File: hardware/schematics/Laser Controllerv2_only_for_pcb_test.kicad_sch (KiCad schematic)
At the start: 116 parts, among them J1 SD Card Module (6-pin, 2.54mm), J2 12.6V IN (BUCK), J3 PWR IN Galvo, J4 FAN1 12V IN, J5 FAN1, J6 FAN2 12V IN, J7 FAN2, U1 ESP32-S3-N16R8-DevKit, U10 DS18B20 connector, U12 OPA4134UA_2K5, U13 Galvo Input, U15 6N137, U16 6N137, U17 6N137, U2 DAC8562SDGST, U3 TTL_RGB Blue, U4 TTL_RGB Red, U5 TTL_RGB Green, U6 DS18B20 connector, U7 DS18B20 connector, U8 DS18B20 connector, U9 DS18B20 connector

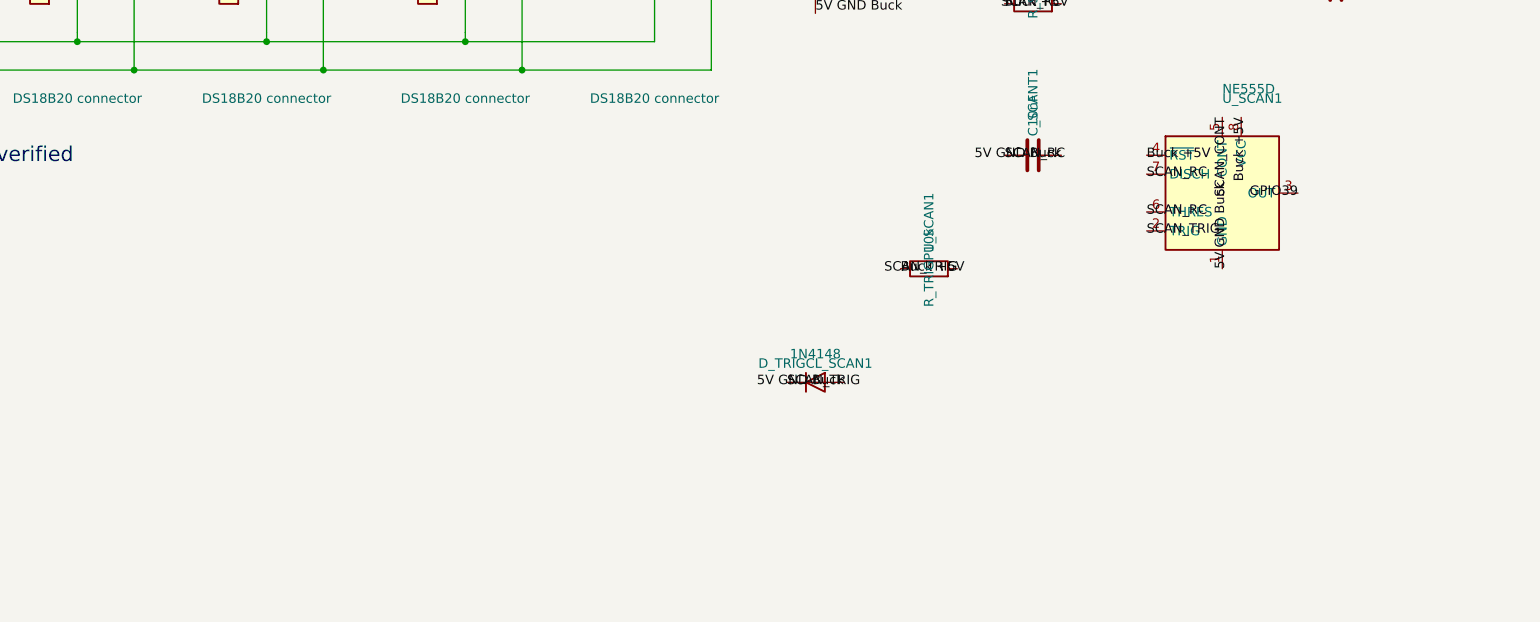
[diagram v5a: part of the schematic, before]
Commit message: fix(hw): buffer scan-status GPIO in v2.0.4
Remove direct 5 V timer drive of GPIO39 while preserving polarity.
Keep the draft unreleased pending safety and physical validation.
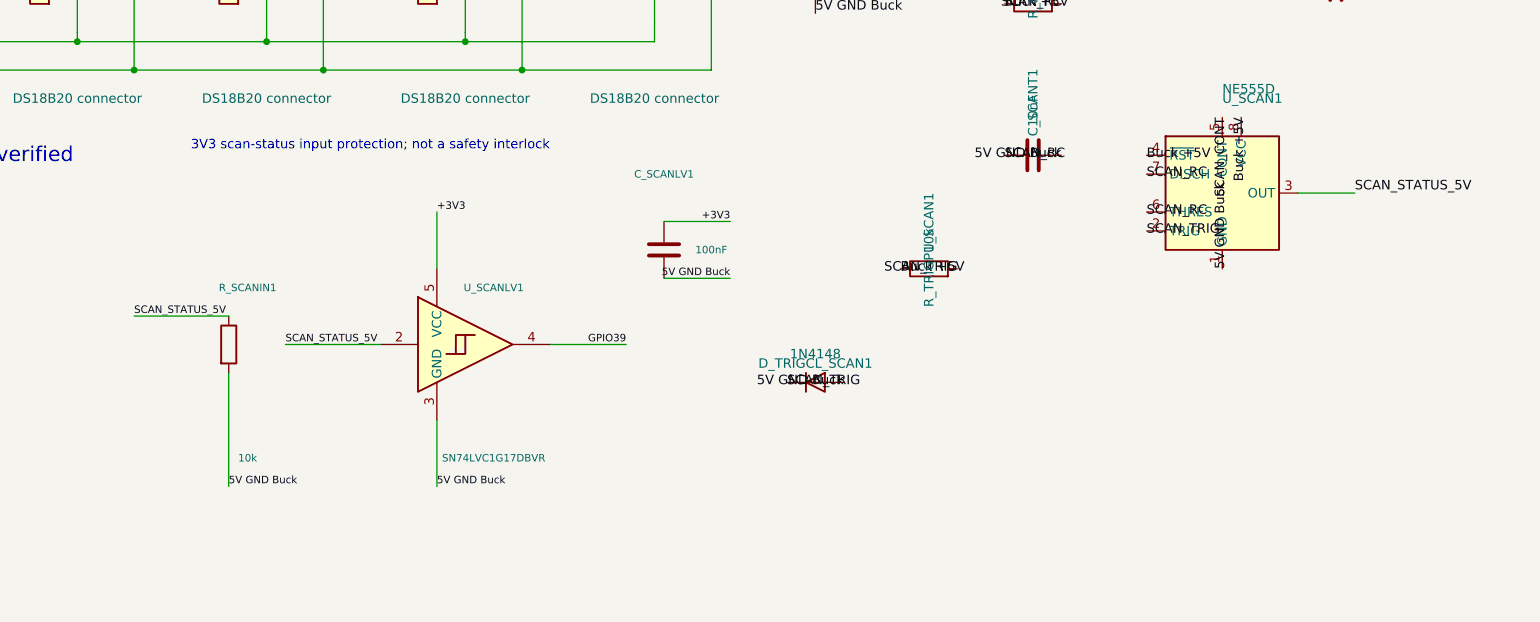
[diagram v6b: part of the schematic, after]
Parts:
- added C_SCANLV1: 100nF, Capacitor_SMD:C_1206_3216Metric, symbol Device:C
- added R_SCANIN1: 10k, Resistor_SMD:R_1206_3216Metric, symbol Device:R
- added U_SCANLV1: SN74LVC1G17DBVR, Package_TO_SOT_SMD:SOT-23-5, symbol 74xGxx:74LVC1G17
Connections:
- net +3V3: now also C_SCANLV1.1, U_SCANLV1.5 (VCC)
- net 5V GND Buck: now also C_SCANLV1.2, R_SCANIN1.2, U_SCANLV1.3 (GND)
- net GPIO39: now also U_SCANLV1.4; no longer U_SCAN1.3 (OUT)
- new net SCAN_STATUS_5V: R_SCANIN1.1, U_SCAN1.3 (OUT), U_SCANLV1.2
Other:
- note added: "3V3 scan-status input protection; not a safety interlock"
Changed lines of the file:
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@@
 		(title "GalvOS ESP32 Laser Controller - V2 engineering review")
 		(date "2026-09-14")
-		(rev "V2.0.3 DRAFT - NOT FOR FABRICATION")
+		(rev "V2.0.4 DRAFT - NOT FOR FABRICATION")
 	)
 	(rectangle
@@
 		)
 	)
-	(label "GPIO39"
-		(at 554.99 330.2 180)
+(label "SCAN_STATUS_5V"
+		(at 562.61 330.2 0)
 		(effects
 			(font
 				(size 1.27 1.27)
 			)
-			(justify right)
+			(justify left bottom)
 		)
 	)
+(wire (pts (xy 554.99 330.2) (xy 562.61 330.2)) (stroke (width 0) (type default)))
 	(label "Buck +5V"
 		(at 389.89 77.47 0)
@@
 		)
 	)
+(symbol (lib_id "74xGxx:74LVC1G17") (at 444.5 350.52 0) (unit 1) (in_bom yes) (on_board yes) (dnp no)
+(property "Reference" "U_SCANLV1" (at 447.04 342.9 0) (effects (font (size 1 1))))
+(property "Value" "SN74LVC1G17DBVR" (at 447.04 365.76 0) (effects (font (size 1 1))))
+(property "Footprint" "Package_TO_SOT_SMD:SOT-23-5" (at 444.5 350.52 0) (hide yes) (effects (font (size 1 1))))
+(property "Datasheet" "https://www.ti.com/lit/ds/symlink/sn74lvc1g17.pdf" (at 444.5 350.52 0) (hide yes) (effects (font (size 1 1))))
+(property "Manufacturer" "Texas Instruments" (at 444.5 350.52 0) (hide yes) (effects (font (size 1 1))))
+(property "MPN" "SN74LVC1G17DBVR" (at 444.5 350.52 0) (hide yes) (effects (font (size 1 1))))
+(property "Layout" "5V-tolerant noninverting buffer; supply from MCU +3V3; local C_SCANLV1 to MCU power ground. Not an independent laser interlock." (at 444.5 350.52 0) (hide yes) (effects (font (size 1 1))))
+(instances (project "Laser Controllerv2_only_for_pcb_test" (path "/d54d297e-dc0d-4b80-be70-d4630411b2f0" (reference "U_SCANLV1") (unit 1)))))
+(symbol (lib_id "Device:R") (at 411.48 350.52 0) (unit 1) (in_bom yes) (on_board yes) (dnp no)
+(property "Reference" "R_SCANIN1" (at 414.02000000000004 342.9 0) (effects (font (size 1 1))))
+(property "Value" "10k" (at 414.02000000000004 365.76 0) (effects (font (size 1 1))))
+(property "Footprint" "Resistor_SMD:R_1206_3216Metric" (at 411.48 350.52 0) (hide yes) (effects (font (size 1 1))))
+(property "Tolerance" "1%" (at 411.48 350.52 0) (hide yes) (effects (font (size 1 1))))
+(property "Power" "0.25W" (at 411.48 350.52 0) (hide yes) (effects (font (size 1 1))))
+(property "Layout" "Bias the buffer input LOW if the timer output is disconnected." (at 411.48 350.52 0) (hide yes) (effects (font (size 1 1))))
+(instances (project "Laser Controllerv2_only_for_pcb_test" (path "/d54d297e-dc0d-4b80-be70-d4630411b2f0" (reference "R_SCANIN1") (unit 1)))))
+(symbol (lib_id "Device:C") (at 469.9 337.82 0) (unit 1) (in_bom yes) (on_board yes) (dnp no)
+(property "Reference" "C_SCANLV1" (at 469.9 327.66 0) (effects (font (size 1 1))))
+(property "Value" "100nF" (at 476.25 337.82 0) (effects (font (size 1 1))))
+(property "Footprint" "Capacitor_SMD:C_1206_3216Metric" (at 469.9 337.82 0) (hide yes) (effects (font (size 1 1))))
+(property "Voltage" "50V" (at 469.9 337.82 0) (hide yes) (effects (font (size 1 1))))
+(property "Dielectric" "X7R" (at 469.9 337.82 0) (hide yes) (effects (font (size 1 1))))
+(property "Tolerance" "10%" (at 469.9 337.82 0) (hide yes) (effects (font (size 1 1))))
+(property "Layout" "Place directly between U_SCANLV1.5 (+3V3) and U_SCANLV1.3 (MCU power ground)." (at 469.9 337.82 0) (hide yes) (effects (font (size 1 1))))
+(instances (project "Laser Controllerv2_only_for_pcb_test" (path "/d54d297e-dc0d-4b80-be70-d4630411b2f0" (reference "C_SCANLV1") (unit 1)))))
+(wire (pts (xy 431.8 350.52) (xy 419.1 350.52)) (stroke (width 0) (type default)))
+(label "SCAN_STATUS_5V" (at 419.1 350.52 0) (effects (font (size 1 1)) (justify left bottom)))
+(wire (pts (xy 454.66 350.52) (xy 464.82 350.52)) (stroke (width 0) (type default)))
+(label "GPIO39" (at 464.82 350.52 180) (effects (font (size 1 1)) (justify right bottom)))
+(wire (pts (xy 439.42 340.36) (xy 439.42 332.74)) (stroke (width 0) (type default)))
+(label "+3V3" (at 439.42 332.74 0) (effects (font (size 1 1)) (justify left bottom)))
+(wire (pts (xy 439.42 360.68) (xy 439.42 369.57)) (stroke (width 0) (type default)))
+(label "5V GND Buck" (at 439.42 369.57 0) (effects (font (size 1 1)) (justify left bottom)))
+(wire (pts (xy 411.48 346.71) (xy 398.78 346.71)) (stroke (width 0) (type default)))
+(label "SCAN_STATUS_5V" (at 398.78 346.71 0) (effects (font (size 1 1)) (justify left bottom)))
+(wire (pts (xy 411.48 354.33) (xy 411.48 369.57)) (stroke (width 0) (type default)))
+(label "5V GND Buck" (at 411.48 369.57 0) (effects (font (size 1 1)) (justify left bottom)))
+(wire (pts (xy 469.9 334.01) (xy 478.79 334.01)) (stroke (width 0) (type default)))
+(label "+3V3" (at 478.79 334.01 180) (effects (font (size 1 1)) (justify right bottom)))
+(wire (pts (xy 469.9 341.63) (xy 478.79 341.63)) (stroke (width 0) (type default)))
+(label "5V GND Buck" (at 478.79 341.63 180) (effects (font (size 1 1)) (justify right bottom)))
+(text "3V3 scan-status input protection; not a safety interlock" (at 406.4 323.85 0) (effects (font (size 1.27 1.27)) (justify left)))
 	(embedded_fonts no)
 	(symbol

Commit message: fix(hw): protect DMX GPIO in v2.0.5
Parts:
- added C_DMXLV1: 100nF, Capacitor_SMD:C_1206_3216Metric, symbol Device:C
- added R_DMXIN1: 10k, Resistor_SMD:R_1206_3216Metric, symbol Device:R
- added U_DMXLV1: SN74LVC1G17DBVR, Package_TO_SOT_SMD:SOT-23-5, symbol 74xGxx:74LVC1G17
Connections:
- net +3V3: now also C_DMXLV1.1, U_DMXLV1.5 (VCC)
- net 5V GND Buck: now also C_DMXLV1.2, R_DMXIN1.2, U_DMXLV1.3 (GND)
- net GPIO4: now also U_DMXLV1.4; no longer J_DMX1.3 (Pin_3)
- new net DMX_RO_5V: J_DMX1.3 (Pin_3), R_DMXIN1.1, U_DMXLV1.2
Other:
- note added: "3V3 DMX input protection; no galvanic isolation"
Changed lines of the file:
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@@
 		(title "GalvOS ESP32 Laser Controller - V2 engineering review")
 		(date "2026-09-14")
-		(rev "V2.0.4 DRAFT - NOT FOR FABRICATION")
+		(rev "V2.0.5 DRAFT - NOT FOR FABRICATION")
 	)
 	(rectangle
@@
 		)
 	)
-	(label "GPIO4"
-		(at 105.41 402.59 0)
-		(effects
-			(font
-				(size 1.27 1.27)
-			)
-			(justify left)
-		)
-	)
+(label "DMX_RO_5V" (at 88.9 402.59 0) (effects (font (size 1 1)) (justify left bottom)))
+(wire (pts (xy 88.9 402.59) (xy 105.41 402.59)) (stroke (width 0) (type default)))
 	(label "FAN2_PWM"
 		(at 236.22 224.79 0)
@@
 		)
 	)
-	(label "Buck +5V"
-		(at 105.41 397.51 0)
-		(effects
-			(font
-				(size 1.27 1.27)
-			)
-			(justify left)
-		)
-	)
+(label "Buck +5V" (at 88.9 397.51 0) (effects (font (size 1 1)) (justify left bottom)))
+(wire (pts (xy 88.9 397.51) (xy 105.41 397.51)) (stroke (width 0) (type default)))
 	(label "SW_BUCK"
 		(at 554.99 116.84 180)
@@
 		)
 	)
-	(label "5V GND Buck"
-		(at 105.41 400.05 0)
-		(effects
-			(font
-				(size 1.27 1.27)
-			)
-			(justify left)
-		)
-	)
+(label "5V GND Buck" (at 88.9 400.05 0) (effects (font (size 1 1)) (justify left bottom)))
+(wire (pts (xy 88.9 400.05) (xy 105.41 400.05)) (stroke (width 0) (type default)))
 	(label "+5V_MCU"
 		(at 187.96 262.89 90)
@@
 		)
 	)
-	(symbol
+(symbol
 		(lib_id "Connector:Conn_01x04_Socket")
 		(at 110.49 400.05 0)
@@
 		)
 	)
+(symbol (lib_id "74xGxx:74LVC1G17") (at 226.06 374.65 0) (unit 1) (in_bom yes) (on_board yes) (dnp no)
+(property "Reference" "U_DMXLV1" (at 228.6 367.03 0) (effects (font (size 1 1))))
+(property "Value" "SN74LVC1G17DBVR" (at 228.6 389.89 0) (effects (font (size 1 1))))
+(property "Footprint" "Package_TO_SOT_SMD:SOT-23-5" (at 226.06 374.65 0) (hide yes) (effects (font (size 1 1))))
+(property "Datasheet" "https://www.ti.com/lit/ds/symlink/sn74lvc1g17.pdf" (at 226.06 374.65 0) (hide yes) (effects (font (size 1 1))))
+(property "Manufacturer" "Texas Instruments" (at 226.06 374.65 0) (hide yes) (effects (font (size 1 1))))
+(property "MPN" "SN74LVC1G17DBVR" (at 226.06 374.65 0) (hide yes) (effects (font (size 1 1))))
+(property "Layout" "5.5V-tolerant noninverting RO buffer, powered by MCU +3V3 with local bypass. Not galvanically isolated; qualify external module and cable." (at 226.06 374.65 0) (hide yes) (effects (font (size 1 1))))
+(instances (project "Laser Controllerv2_only_for_pcb_test" (path "/d54d297e-dc0d-4b80-be70-d4630411b2f0" (reference "U_DMXLV1") (unit 1)))))
+(symbol (lib_id "Device:R") (at 193.04 374.65 0) (unit 1) (in_bom yes) (on_board yes) (dnp no)
+(property "Reference" "R_DMXIN1" (at 193.04 365.76 0) (effects (font (size 1 1))))
+(property "Value" "10k" (at 187.96 374.65 0) (effects (font (size 1 1))))
+(property "Footprint" "Resistor_SMD:R_1206_3216Metric" (at 193.04 374.65 0) (hide yes) (effects (font (size 1 1))))
+(property "Tolerance" "1%" (at 193.04 374.65 0) (hide yes) (effects (font (size 1 1))))
+(property "Power" "0.25W" (at 193.04 374.65 0) (hide yes) (effects (font (size 1 1))))
+(property "Layout" "Pull RO-side input LOW when disconnected; UART sees break/no valid packet, not idle HIGH. Does not provide laser shutdown." (at 193.04 374.65 0) (hide yes) (effects (font (size 1 1))))
+(instances (project "Laser Controllerv2_only_for_pcb_test" (path "/d54d297e-dc0d-4b80-be70-d4630411b2f0" (reference "R_DMXIN1") (unit 1)))))
+(symbol (lib_id "Device:C") (at 251.46 361.95 0) (unit 1) (in_bom yes) (on_board yes) (dnp no)
+(property "Reference" "C_DMXLV1" (at 251.46 351.79 0) (effects (font (size 1 1))))
+(property "Value" "100nF" (at 257.81 361.95 0) (effects (font (size 1 1))))
+(property "Footprint" "Capacitor_SMD:C_1206_3216Metric" (at 251.46 361.95 0) (hide yes) (effects (font (size 1 1))))
+(property "Voltage" "50V" (at 251.46 361.95 0) (hide yes) (effects (font (size 1 1))))
+(property "Dielectric" "X7R" (at 251.46 361.95 0) (hide yes) (effects (font (size 1 1))))
+(property "Tolerance" "10%" (at 251.46 361.95 0) (hide yes) (effects (font (size 1 1))))
+(property "Layout" "Place directly between U_DMXLV1.5 (+3V3) and U_DMXLV1.3 (MCU power ground)." (at 251.46 361.95 0) (hide yes) (effects (font (size 1 1))))
+(instances (project "Laser Controllerv2_only_for_pcb_test" (path "/d54d297e-dc0d-4b80-be70-d4630411b2f0" (reference "C_DMXLV1") (unit 1)))))
+(wire (pts (xy 213.36 374.65) (xy 200.66 374.65)) (stroke (width 0) (type default)))
+(label "DMX_RO_5V" (at 200.66 374.65 0) (effects (font (size 1 1)) (justify left bottom)))
+(wire (pts (xy 236.22 374.65) (xy 246.38 374.65)) (stroke (width 0) (type default)))
+(label "GPIO4" (at 246.38 374.65 180) (effects (font (size 1 1)) (justify right bottom)))
+(wire (pts (xy 220.98 364.49) (xy 220.98 356.87)) (stroke (width 0) (type default)))
+(label "+3V3" (at 220.98 356.87 0) (effects (font (size 1 1)) (justify left bottom)))
+(wire (pts (xy 220.98 384.81) (xy 220.98 393.7)) (stroke (width 0) (type default)))
+(label "5V GND Buck" (at 220.98 393.7 0) (effects (font (size 1 1)) (justify left bottom)))
+(wire (pts (xy 193.04 370.84) (xy 180.34 370.84)) (stroke (width 0) (type default)))
+(label "DMX_RO_5V" (at 180.34 370.84 0) (effects (font (size 1 1)) (justify left bottom)))
+(wire (pts (xy 193.04 378.46) (xy 193.04 393.7)) (stroke (width 0) (type default)))
+(label "5V GND Buck" (at 193.04 393.7 0) (effects (font (size 1 1)) (justify left bottom)))
+(wire (pts (xy 251.46 358.14) (xy 260.35 358.14)) (stroke (width 0) (type default)))
+(label "+3V3" (at 260.35 358.14 180) (effects (font (size 1 1)) (justify right bottom)))
+(wire (pts (xy 251.46 365.76) (xy 260.35 365.76)) (stroke (width 0) (type default)))
+(label "5V GND Buck" (at 260.35 365.76 180) (effects (font (size 1 1)) (justify right bottom)))
+(text "3V3 DMX input protection; no galvanic isolation" (at 187.96 346.71 0) (effects (font (size 1.27 1.27)) (justify left)))
 	(symbol
 		(lib_id "Diode:1N4148")

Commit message: fix(hw): shorten buck feedback in v2.0.6
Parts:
- C_BOOT1: Dielectric (none) -> X7R; Layout (none) -> Short, wide BOOT-to-SW connections; ceramic 100nF, TI minim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; Tolerance (none) -> 10%; Voltage (none) -> 16V
- C_INHF1: value 100nF -> 220nF; Dielectric (none) -> X7R; Layout (none) -> 220nF input HF bypass per TI SNVSAN3F section 9.2.2.6; shor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; Tolerance (none) -> 10%; Voltage (none) -> 50V
- C_VCC1: Dielectric (none) -> X7R; Layout (none) -> Local 1uF VCC-to-power-ground bypass per TI SNVSAN3F sectio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; Tolerance (none) -> 10%; Voltage (none) -> 16V
- R_FB1: Layout (none) -> Place divider close to U_BUCK1 FB pin; keep FB short and VO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; Tolerance (none) -> 1%
- R_FB2: Layout (none) -> Short FB connection and quiet local return to U_BUCK1 expos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; Tolerance (none) -> 1%
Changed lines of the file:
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@@
 		(title "GalvOS ESP32 Laser Controller - V2 engineering review")
 		(date "2026-09-14")
-		(rev "V2.0.5 DRAFT - NOT FOR FABRICATION")
+		(rev "V2.0.6 DRAFT - NOT FOR FABRICATION")
 	)
 	(rectangle
@@
 			)
 		)
+		(property "Tolerance" "1%"
+			(at 393.7 77.47 0)
+			(hide yes)
+			(effects (font (size 1.27 1.27)))
+		)
+		(property "Layout" "Place divider close to U_BUCK1 FB pin; keep FB short and VOUT sense away from SW."
+			(at 393.7 77.47 0)
+			(hide yes)
+			(effects (font (size 1.27 1.27)))
+		)
 		(pin "1"
 		)
@@
 			)
 		)
+		(property "Tolerance" "1%"
+			(at 393.7 92.71 0)
+			(hide yes)
+			(effects (font (size 1.27 1.27)))
+		)
+		(property "Layout" "Short FB connection and quiet local return to U_BUCK1 exposed-pad ground."
+			(at 393.7 92.71 0)
+			(hide yes)
+			(effects (font (size 1.27 1.27)))
+		)
 		(pin "1"
 		)
@@
 			)
 		)
+		(property "Voltage" "16V"
+			(at 529.59 80.01 0)
+			(hide yes)
+			(effects (font (size 1.27 1.27)))
+		)
+		(property "Dielectric" "X7R"
+			(at 529.59 80.01 0)
+			(hide yes)
+			(effects (font (size 1.27 1.27)))
+		)
+		(property "Tolerance" "10%"
+			(at 529.59 80.01 0)
+			(hide yes)
+			(effects (font (size 1.27 1.27)))
+		)
+		(property "Layout" "Local 1uF VCC-to-power-ground bypass per TI SNVSAN3F section 9.2.2.8."
+			(at 529.59 80.01 0)
+			(hide yes)
+			(effects (font (size 1.27 1.27)))
+		)
 		(pin "1"
 		)
@@
 			)
 		)
-		(property "Value" "100nF"
+		(property "Value" "220nF"
 			(at 515.62 124.46000000000001 0)
 			(show_name no)
@@
 			)
 		)
+		(property "Voltage" "50V"
+			(at 515.62 129.54 0)
+			(hide yes)
+			(effects (font (size 1.27 1.27)))
+		)
+		(property "Dielectric" "X7R"
+			(at 515.62 129.54 0)
+			(hide yes)
+			(effects (font (size 1.27 1.27)))
+		)
+		(property "Tolerance" "10%"
+			(at 515.62 129.54 0)
+			(hide yes)
+			(effects (font (size 1.27 1.27)))
+		)
+		(property "Layout" "220nF input HF bypass per TI SNVSAN3F section 9.2.2.6; short VIN/PGND loop."
+			(at 515.62 129.54 0)
+			(hide yes)
+			(effects (font (size 1.27 1.27)))
+		)
 		(pin "1"
 		)
@@
 			)
 		)
+		(property "Voltage" "16V"
+			(at 364.49 27.94 0)
+			(hide yes)
+			(effects (font (size 1.27 1.27)))
+		)
+		(property "Dielectric" "X7R"
+			(at 364.49 27.94 0)
+			(hide yes)
+			(effects (font (size 1.27 1.27)))
+		)
+		(property "Tolerance" "10%"
+			(at 364.49 27.94 0)
+			(hide yes)
+			(effects (font (size 1.27 1.27)))
+		)
+		(property "Layout" "Short, wide BOOT-to-SW connections; ceramic 100nF, TI minimum 10V."
+			(at 364.49 27.94 0)
+			(hide yes)
+			(effects (font (size 1.27 1.27)))
+		)
 		(pin "1"
